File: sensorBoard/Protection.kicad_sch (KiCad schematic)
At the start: 8 parts

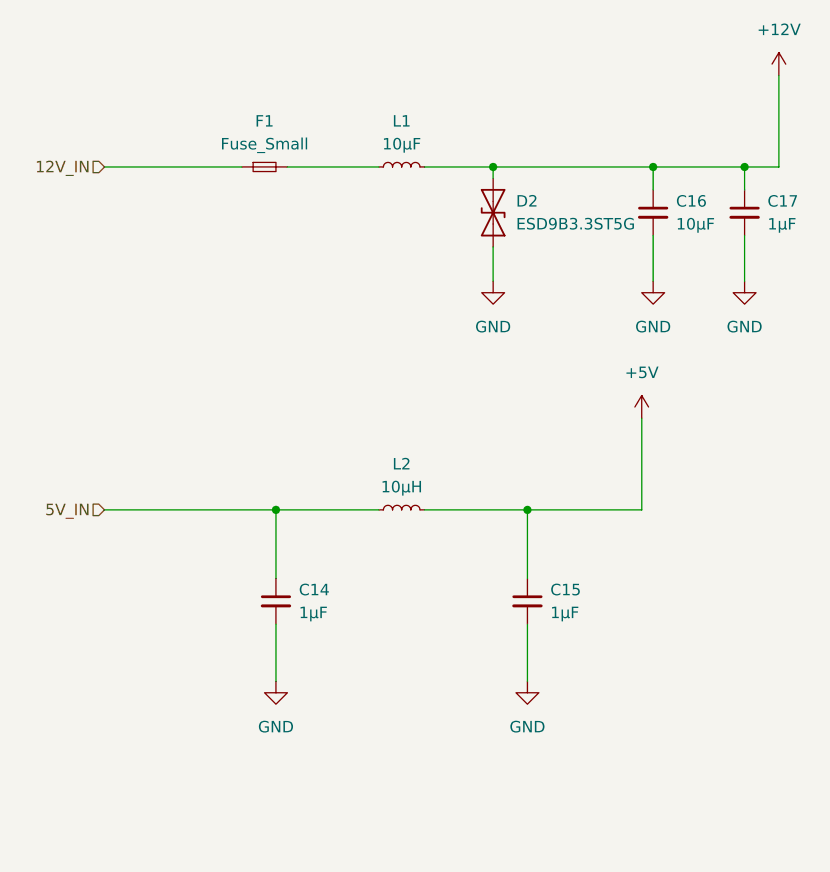
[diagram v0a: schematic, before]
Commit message: added the footprints, connectors left
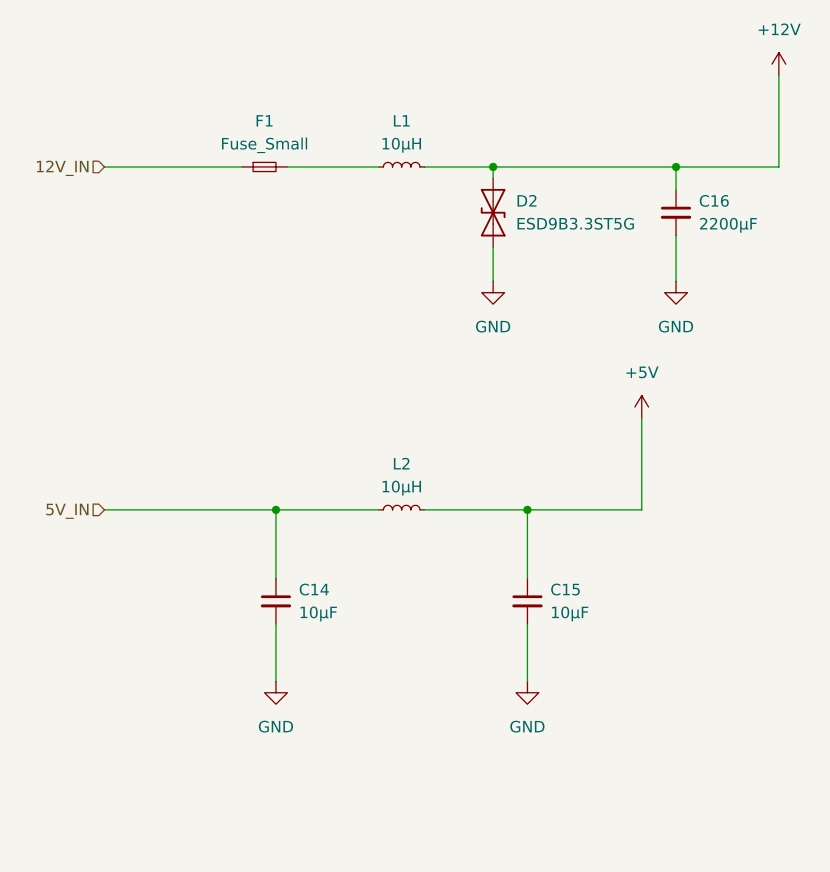
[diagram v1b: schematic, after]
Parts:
- removed C17: 1µF, symbol Device:C_Small
- C14, C15: value 1µF -> 10µF; footprint (none) -> Capacitor_SMD:C_1210_3225Metric
- C16: value 10µF -> 2200µF; footprint (none) -> Capacitor_SMD:CP_Elec_18x17.5
- F1: footprint (none) -> Inductor_SMD:L_Cenker_CKCS8080
- L1: value 10µF -> 10µH; footprint (none) -> Inductor_SMD:L_Coilcraft_XAL1580-612
- L2: footprint (none) -> Inductor_SMD:L_Bourns_SRP1245A
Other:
- moved on the sheet: C16
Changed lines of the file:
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@@
 	(paper "A4")
 	(junction
-		(at 134.62 50.8)
+		(at 127 50.8)
 		(diameter 0)
 		(color 0 0 0 0)
@@
 	)
 	(junction
-		(at 124.46 50.8)
-		(diameter 0)
-		(color 0 0 0 0)
-	)
-	(junction
 		(at 106.68 50.8)
 		(diameter 0)
@@
 	(wire
 		(pts
-			(xy 106.68 50.8) (xy 124.46 50.8)
+			(xy 106.68 50.8) (xy 127 50.8)
 		)
 		(stroke
@@
 	(wire
 		(pts
-			(xy 124.46 58.42) (xy 124.46 63.5)
+			(xy 127 58.42) (xy 127 63.5)
 		)
 		(stroke
@@
 	(wire
 		(pts
-			(xy 134.62 58.42) (xy 134.62 63.5)
-		)
-		(stroke
-			(width 0)
-			(type default)
-		)
-	)
-	(wire
-		(pts
 			(xy 63.5 88.9) (xy 82.55 88.9)
 		)
@@
 	(wire
 		(pts
-			(xy 124.46 50.8) (xy 124.46 53.34)
+			(xy 127 50.8) (xy 127 53.34)
 		)
 		(stroke
@@
 	(wire
 		(pts
-			(xy 124.46 50.8) (xy 134.62 50.8)
+			(xy 127 50.8) (xy 138.43 50.8)
 		)
 		(stroke
@@
 		(pts
 			(xy 106.68 50.8) (xy 106.68 52.07)
-		)
-		(stroke
-			(width 0)
-			(type default)
-		)
-	)
-	(wire
-		(pts
-			(xy 134.62 50.8) (xy 138.43 50.8)
-		)
-		(stroke
-			(width 0)
-			(type default)
-		)
-	)
-	(wire
-		(pts
-			(xy 134.62 50.8) (xy 134.62 53.34)
 		)
 		(stroke
@@
 			)
 		)
-		(property "Footprint" ""
+		(property "Footprint" "Inductor_SMD:L_Bourns_SRP1245A"
 			(at 96.52 88.9 0)
 			(effects
@@
 			)
 		)
-		(property "Datasheet" "~"
+		(property "Datasheet" "https://www.mouser.de/ProductDetail/Wurth-Elektronik/784771100?qs=sBf%2Fb4nBSles1UUNhM1nwg%3D%3D"
 			(at 96.52 88.9 0)
 			(effects
@@
 	)
 	(symbol
-		(lib_id "Device:C_Small")
-		(at 134.62 55.88 0)
-		(unit 1)
-		(exclude_from_sim no)
-		(in_bom yes)
-		(on_board yes)
-		(dnp no)
-		(fields_autoplaced yes)
-		(property "Reference" "C17"
-			(at 137.16 54.6162 0)
-			(effects
-				(font
-					(size 1.27 1.27)
-				)
-				(justify left)
-			)
-		)
-		(property "Value" "1µF"
-			(at 137.16 57.1562 0)
-			(effects
-				(font
-					(size 1.27 1.27)
-				)
-				(justify left)
-			)
-		)
-		(property "Footprint" ""
-			(at 134.62 55.88 0)
-			(effects
-				(font
-					(size 1.27 1.27)
-				)
-				(hide yes)
-			)
-		)
-		(property "Datasheet" "~"
-			(at 134.62 55.88 0)
-			(effects
-				(font
-					(size 1.27 1.27)
-				)
-				(hide yes)
-			)
-		)
-		(property "Description" "Unpolarized capacitor, small symbol"
-			(at 134.62 55.88 0)
-			(effects
-				(font
-					(size 1.27 1.27)
-				)
-				(hide yes)
-			)
-		)
-		(pin "2"
-		)
-		(pin "1"
-		)
-		(instances
-			(project "sensorBoard"
-				(path "/df1584e9-54f0-49dc-b423-5f64048efa01/eeb71e0f-46bb-44dd-988f-3e7d2427e332"
-					(reference "C17")
-					(unit 1)
-				)
-			)
-		)
-	)
-	(symbol
 		(lib_id "power:GND")
 		(at 110.49 107.95 0)
@@
 	)
 	(symbol
-		(lib_id "power:GND")
-		(at 134.62 63.5 0)
-		(unit 1)
-		(exclude_from_sim no)
-		(in_bom yes)
-		(on_board yes)
-		(dnp no)
-		(fields_autoplaced yes)
-		(property "Reference" "#PWR051"
-			(at 134.62 69.85 0)
-			(effects
-				(font
-					(size 1.27 1.27)
-				)
-				(hide yes)
-			)
-		)
-		(property "Value" "GND"
-			(at 134.62 68.58 0)
-			(effects
-				(font
-					(size 1.27 1.27)
-				)
-			)
-		)
-		(property "Footprint" ""
-			(at 134.62 63.5 0)
-			(effects
-				(font
-					(size 1.27 1.27)
-				)
-				(hide yes)
-			)
-		)
-		(property "Datasheet" ""
-			(at 134.62 63.5 0)
-			(effects
-				(font
-					(size 1.27 1.27)
-				)
-				(hide yes)
-			)
-		)
-		(property "Description" "Power symbol creates a global label with name \"GND\" , ground"
-			(at 134.62 63.5 0)
-			(effects
-				(font
-					(size 1.27 1.27)
-				)
-				(hide yes)
-			)
-		)
-		(pin "1"
-		)
-		(instances
-			(project ""
-				(path "/df1584e9-54f0-49dc-b423-5f64048efa01/eeb71e0f-46bb-44dd-988f-3e7d2427e332"
-					(reference "#PWR051")
-					(unit 1)
-				)
-			)
-		)
-	)
-	(symbol
 		(lib_id "Device:C_Small")
 		(at 110.49 99.06 0)
@@
 			)
 		)
-		(property "Value" "1µF"
+		(property "Value" "10µF"
 			(at 113.03 100.3362 0)
 			(effects
@@
 			)
 		)
-		(property "Footprint" ""
+		(property "Footprint" "Capacitor_SMD:C_1210_3225Metric"
 			(at 110.49 99.06 0)
 			(effects
@@
 	(symbol
 		(lib_id "power:GND")
-		(at 124.46 63.5 0)
+		(at 127 63.5 0)
 		(unit 1)
 		(exclude_from_sim no)
@@
 		(fields_autoplaced yes)
 		(property "Reference" "#PWR050"
-			(at 124.46 69.85 0)
+			(at 127 69.85 0)
 			(effects
 				(font
@@
 		)
 		(property "Value" "GND"
-			(at 124.46 68.58 0)
+			(at 127 68.58 0)
 			(effects
 				(font
@@
 		)
 		(property "Footprint" ""
-			(at 124.46 63.5 0)
+			(at 127 63.5 0)
 			(effects
 				(font
@@
 		)
 		(property "Datasheet" ""
-			(at 124.46 63.5 0)
+			(at 127 63.5 0)
 			(effects
 				(font
@@
 		)
 		(property "Description" "Power symbol creates a global label with name \"GND\" , ground"
-			(at 124.46 63.5 0)
+			(at 127 63.5 0)
 			(effects
 				(font
@@
 			)
 		)
-		(property "Value" "10µF"
+		(property "Value" "10µH"
 			(at 96.52 48.26 90)
 			(effects
@@
 			)
 		)
-		(property "Footprint" ""
+		(property "Footprint" "Inductor_SMD:L_Coilcraft_XAL1580-612"
 			(at 96.52 50.8 0)
 			(effects
@@
 			)
 		)
-		(property "Datasheet" "~"
+		(property "Datasheet" "https://www.mouser.de/ProductDetail/Wurth-Elektronik/78439370100?qs=Znm5pLBrcALJdf%2F0qW3A9g%3D%3D"
 			(at 96.52 50.8 0)
 			(effects
@@
 			)
 		)
-		(property "Value" "1µF"
+		(property "Value" "10µF"
 			(at 85.09 100.3362 0)
 			(effects
@@
 			)
 		)
-		(property "Footprint" ""
+		(property "Footprint" "Capacitor_SMD:C_1210_3225Metric"
 			(at 82.55 99.06 0)
 			(effects
@@
 	(symbol
 		(lib_id "Device:C_Small")
-		(at 124.46 55.88 0)
+		(at 127 55.88 0)
 		(unit 1)
 		(exclude_from_sim no)
@@
 		(fields_autoplaced yes)
 		(property "Reference" "C16"
-			(at 127 54.6162 0)
+			(at 129.54 54.6162 0)
 			(effects
 				(font
@@
 			)
 		)
-		(property "Value" "10µF"
-			(at 127 57.1562 0)
+		(property "Value" "2200µF"
+			(at 129.54 57.1562 0)
 			(effects
 				(font
@@
 			)
 		)
-		(property "Footprint" ""
-			(at 124.46 55.88 0)
-			(effects
-				(font
-					(size 1.27 1.27)
-				)
-				(hide yes)
-			)
-		)
-		(property "Datasheet" "~"
-			(at 124.46 55.88 0)
+		(property "Footprint" "Capacitor_SMD:CP_Elec_18x17.5"
+			(at 127 55.88 0)
+			(effects
+				(font
+					(size 1.27 1.27)
+				)
+				(hide yes)
+			)
+		)
+		(property "Datasheet" "https://www.mouser.de/ProductDetail/KYOCERA-AVX/AEA1616222M025R?qs=sGAEpiMZZMvwFf0viD3Y3bXvgfG2gej7kz4%2FvdnjV6VRoSXP%252BAJg9A%3D%3D"
+			(at 127 55.88 0)
 			(effects
 				(font
@@
 		)
 		(property "Description" "Unpolarized capacitor, small symbol"
-			(at 124.46 55.88 0)
+			(at 127 55.88 0)
 			(effects
 				(font
@@
 			)
 		)
-		(property "Footprint" ""
+		(property "Footprint" "Inductor_SMD:L_Cenker_CKCS8080"
 			(at 81.28 50.8 0)
 			(effects
@@
 			)
 		)
-		(property "Datasheet" "~"
+		(property "Datasheet" "https://www.mouser.de/ProductDetail/Wurth-Elektronik/78439370100?qs=Znm5pLBrcALJdf%2F0qW3A9g%3D%3D"
 			(at 81.28 50.8 0)
 			(effects

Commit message: started the layout
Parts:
- D2: footprint Diode_SMD:D_SOD-923 -> Diode_SMD:D_SMB
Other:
- moved on the sheet: C14, C15, L2
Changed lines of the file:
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@@
 	)
 	(junction
-		(at 110.49 88.9)
+		(at 121.92 101.6)
 		(diameter 0)
 		(color 0 0 0 0)
@@
 	)
 	(junction
-		(at 82.55 88.9)
+		(at 93.98 101.6)
 		(diameter 0)
 		(color 0 0 0 0)
@@
 	(wire
 		(pts
-			(xy 82.55 88.9) (xy 93.98 88.9)
+			(xy 93.98 101.6) (xy 105.41 101.6)
 		)
 		(stroke
@@
 	(wire
 		(pts
-			(xy 110.49 88.9) (xy 123.19 88.9)
+			(xy 121.92 101.6) (xy 134.62 101.6)
 		)
 		(stroke
@@
 	(wire
 		(pts
-			(xy 63.5 88.9) (xy 82.55 88.9)
-		)
-		(stroke
-			(width 0)
-			(type default)
-		)
-	)
-	(wire
-		(pts
-			(xy 99.06 88.9) (xy 110.49 88.9)
-		)
-		(stroke
-			(width 0)
-			(type default)
-		)
-	)
-	(wire
-		(pts
-			(xy 82.55 88.9) (xy 82.55 96.52)
+			(xy 74.93 101.6) (xy 93.98 101.6)
+		)
+		(stroke
+			(width 0)
+			(type default)
+		)
+	)
+	(wire
+		(pts
+			(xy 110.49 101.6) (xy 121.92 101.6)
+		)
+		(stroke
+			(width 0)
+			(type default)
+		)
+	)
+	(wire
+		(pts
+			(xy 93.98 101.6) (xy 93.98 109.22)
 		)
 		(stroke
@@
 	(wire
 		(pts
-			(xy 110.49 88.9) (xy 110.49 96.52)
-		)
-		(stroke
-			(width 0)
-			(type default)
-		)
-	)
-	(wire
-		(pts
-			(xy 82.55 101.6) (xy 82.55 107.95)
+			(xy 121.92 101.6) (xy 121.92 109.22)
+		)
+		(stroke
+			(width 0)
+			(type default)
+		)
+	)
+	(wire
+		(pts
+			(xy 93.98 114.3) (xy 93.98 120.65)
 		)
 		(stroke
@@
 	(wire
 		(pts
-			(xy 123.19 88.9) (xy 123.19 78.74)
+			(xy 134.62 101.6) (xy 134.62 91.44)
 		)
 		(stroke
@@
 	(wire
 		(pts
-			(xy 110.49 101.6) (xy 110.49 107.95)
+			(xy 121.92 114.3) (xy 121.92 120.65)
 		)
 		(stroke
@@
 	(hierarchical_label "5V_IN"
 		(shape input)
-		(at 63.5 88.9 180)
+		(at 74.93 101.6 180)
 		(fields_autoplaced yes)
 		(effects
@@
 	(symbol
 		(lib_id "Device:L_Small")
-		(at 96.52 88.9 90)
+		(at 107.95 101.6 90)
 		(unit 1)
 		(exclude_from_sim no)
@@
 		(fields_autoplaced yes)
 		(property "Reference" "L2"
-			(at 96.52 83.82 90)
+			(at 107.95 96.52 90)
 			(effects
 				(font
@@
 		)
 		(property "Value" "10µH"
-			(at 96.52 86.36 90)
+			(at 107.95 99.06 90)
 			(effects
 				(font
@@
 		)
 		(property "Footprint" "Inductor_SMD:L_Bourns_SRP1245A"
-			(at 96.52 88.9 0)
+			(at 107.95 101.6 0)
 			(effects
 				(font
@@
 		)
 		(property "Datasheet" "https://www.mouser.de/ProductDetail/Wurth-Elektronik/784771100?qs=sBf%2Fb4nBSles1UUNhM1nwg%3D%3D"
-			(at 96.52 88.9 0)
+			(at 107.95 101.6 0)
 			(effects
 				(font
@@
 		)
 		(property "Description" "Inductor, small symbol"
-			(at 96.52 88.9 0)
+			(at 107.95 101.6 0)
 			(effects
 				(font
@@
 	(symbol
 		(lib_id "power:GND")
-		(at 110.49 107.95 0)
+		(at 121.92 120.65 0)
 		(unit 1)
 		(exclude_from_sim no)
@@
 		(fields_autoplaced yes)
 		(property "Reference" "#PWR049"
-			(at 110.49 114.3 0)
+			(at 121.92 127 0)
 			(effects
 				(font
@@
 		)
 		(property "Value" "GND"
-			(at 110.49 113.03 0)
+			(at 121.92 125.73 0)
 			(effects
 				(font
@@
 		)
 		(property "Footprint" ""
-			(at 110.49 107.95 0)
+			(at 121.92 120.65 0)
 			(effects
 				(font
@@
 		)
 		(property "Datasheet" ""
-			(at 110.49 107.95 0)
+			(at 121.92 120.65 0)
 			(effects
 				(font
@@
 		)
 		(property "Description" "Power symbol creates a global label with name \"GND\" , ground"
-			(at 110.49 107.95 0)
+			(at 121.92 120.65 0)
 			(effects
 				(font
@@
 	(symbol
 		(lib_id "Device:C_Small")
-		(at 110.49 99.06 0)
+		(at 121.92 111.76 0)
 		(unit 1)
 		(exclude_from_sim no)
@@
 		(fields_autoplaced yes)
 		(property "Reference" "C15"
-			(at 113.03 97.7962 0)
+			(at 124.46 110.4962 0)
 			(effects
 				(font
@@
 		)
 		(property "Value" "10µF"
-			(at 113.03 100.3362 0)
+			(at 124.46 113.0362 0)
 			(effects
 				(font
@@
 		)
 		(property "Footprint" "Capacitor_SMD:C_1210_3225Metric"
-			(at 110.49 99.06 0)
+			(at 121.92 111.76 0)
 			(effects
 				(font
@@
 		)
 		(property "Datasheet" "~"
-			(at 110.49 99.06 0)
+			(at 121.92 111.76 0)
 			(effects
 				(font
@@
 		)
 		(property "Description" "Unpolarized capacitor, small symbol"
-			(at 110.49 99.06 0)
+			(at 121.92 111.76 0)
 			(effects
 				(font
@@
 	(symbol
 		(lib_id "power:GND")
-		(at 82.55 107.95 0)
+		(at 93.98 120.65 0)
 		(unit 1)
 		(exclude_from_sim no)
@@
 		(fields_autoplaced yes)
 		(property "Reference" "#PWR048"
-			(at 82.55 114.3 0)
+			(at 93.98 127 0)
 			(effects
 				(font
@@
 		)
 		(property "Value" "GND"
-			(at 82.55 113.03 0)
+			(at 93.98 125.73 0)
 			(effects
 				(font
@@
 		)
 		(property "Footprint" ""
-			(at 82.55 107.95 0)
+			(at 93.98 120.65 0)
 			(effects
 				(font
@@
 		)
 		(property "Datasheet" ""
-			(at 82.55 107.95 0)
+			(at 93.98 120.65 0)
 			(effects
 				(font
@@
 		)
 		(property "Description" "Power symbol creates a global label with name \"GND\" , ground"
-			(at 82.55 107.95 0)
+			(at 93.98 120.65 0)
 			(effects
 				(font
@@
 			)
 		)
-		(property "Footprint" "Diode_SMD:D_SOD-923"
+		(property "Footprint" "Diode_SMD:D_SMB"
 			(at 106.68 55.88 0)
 			(effects
@@
 			)
 		)
-		(property "Datasheet" "https://www.onsemi.com/pub/Collateral/ESD9B-D.PDF"
+		(property "Datasheet" "https://www.mouser.de/ProductDetail/Littelfuse/SMBJ13A?qs=HR2RnyOI4E7jYyaNBU0w0w%3D%3D&srsltid=AfmBOor6_agX3vir1GVOfC2EUzzLngFgs9YFDGWrTlkz9UynbndBGqlu"
 			(at 106.68 55.88 0)
 			(effects
@@
 	(symbol
 		(lib_id "Device:C_Small")
-		(at 82.55 99.06 0)
+		(at 93.98 111.76 0)
 		(unit 1)
 		(exclude_from_sim no)
@@
 		(fields_autoplaced yes)
 		(property "Reference" "C14"
-			(at 85.09 97.7962 0)
+			(at 96.52 110.4962 0)
 			(effects
 				(font
@@
 		)
 		(property "Value" "10µF"
-			(at 85.09 100.3362 0)
+			(at 96.52 113.0362 0)
 			(effects
 				(font
@@
 		)
 		(property "Footprint" "Capacitor_SMD:C_1210_3225Metric"
-			(at 82.55 99.06 0)
+			(at 93.98 111.76 0)
 			(effects
 				(font
@@
 		)
 		(property "Datasheet" "~"
-			(at 82.55 99.06 0)
+			(at 93.98 111.76 0)
 			(effects
 				(font
@@
 		)
 		(property "Description" "Unpolarized capacitor, small symbol"
-			(at 82.55 99.06 0)
+			(at 93.98 111.76 0)
 			(effects
 				(font
@@
 	(symbol
 		(lib_id "power:+5V")
-		(at 123.19 78.74 0)
+		(at 134.62 91.44 0)
 		(unit 1)
 		(exclude_from_sim no)
@@
 		(fields_autoplaced yes)
 		(property "Reference" "#PWR047"
-			(at 123.19 82.55 0)
+			(at 134.62 95.25 0)
 			(effects
 				(font
@@
 		)
 		(property "Value" "+5V"
-			(at 123.19 73.66 0)
+			(at 134.62 86.36 0)
 			(effects
 				(font
@@
 		)
 		(property "Footprint" ""
-			(at 123.19 78.74 0)
+			(at 134.62 91.44 0)
 			(effects
 				(font
@@
 		)
 		(property "Datasheet" ""
-			(at 123.19 78.74 0)
+			(at 134.62 91.44 0)
 			(effects
 				(font
@@
 		)
 		(property "Description" "Power symbol creates a global label with name \"+5V\""
-			(at 123.19 78.74 0)
-			(effects
-				(font
+			(at 134.62 91.44 0)
+			(effects
+				(font
